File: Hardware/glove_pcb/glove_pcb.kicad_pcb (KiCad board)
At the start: 2 copper layers, 150 x 150 mm, 106 parts, among them J1 Barrel_Jack_Switch, J10 ICSP, J11 IMU, J12 IMU, J13 Conn_01x01, J2 Conn_01x02, J3 Conn_01x02, J4 Conn_01x02, J5 Conn_01x02, J6 Conn_01x02, J7 Potentiometers, J8 Potentiometers, J9 Debug Serial, U1 AP63205WU, U10 MCP3008, U11 MCP3008, U12 BM70BLES1FC2-0B04AA, U13 74LVC1T45GW_125, U14 74LVC1T45GW_125, U2 TCR2EF33_LMCT, U3 DRV8876PWPR, U4 DRV8876PWPR, U5 DRV8876PWPR, U6 DRV8876PWPR, U7 DRV8876PWPR, U8 MCP3008, U9 ATmega328PB-A

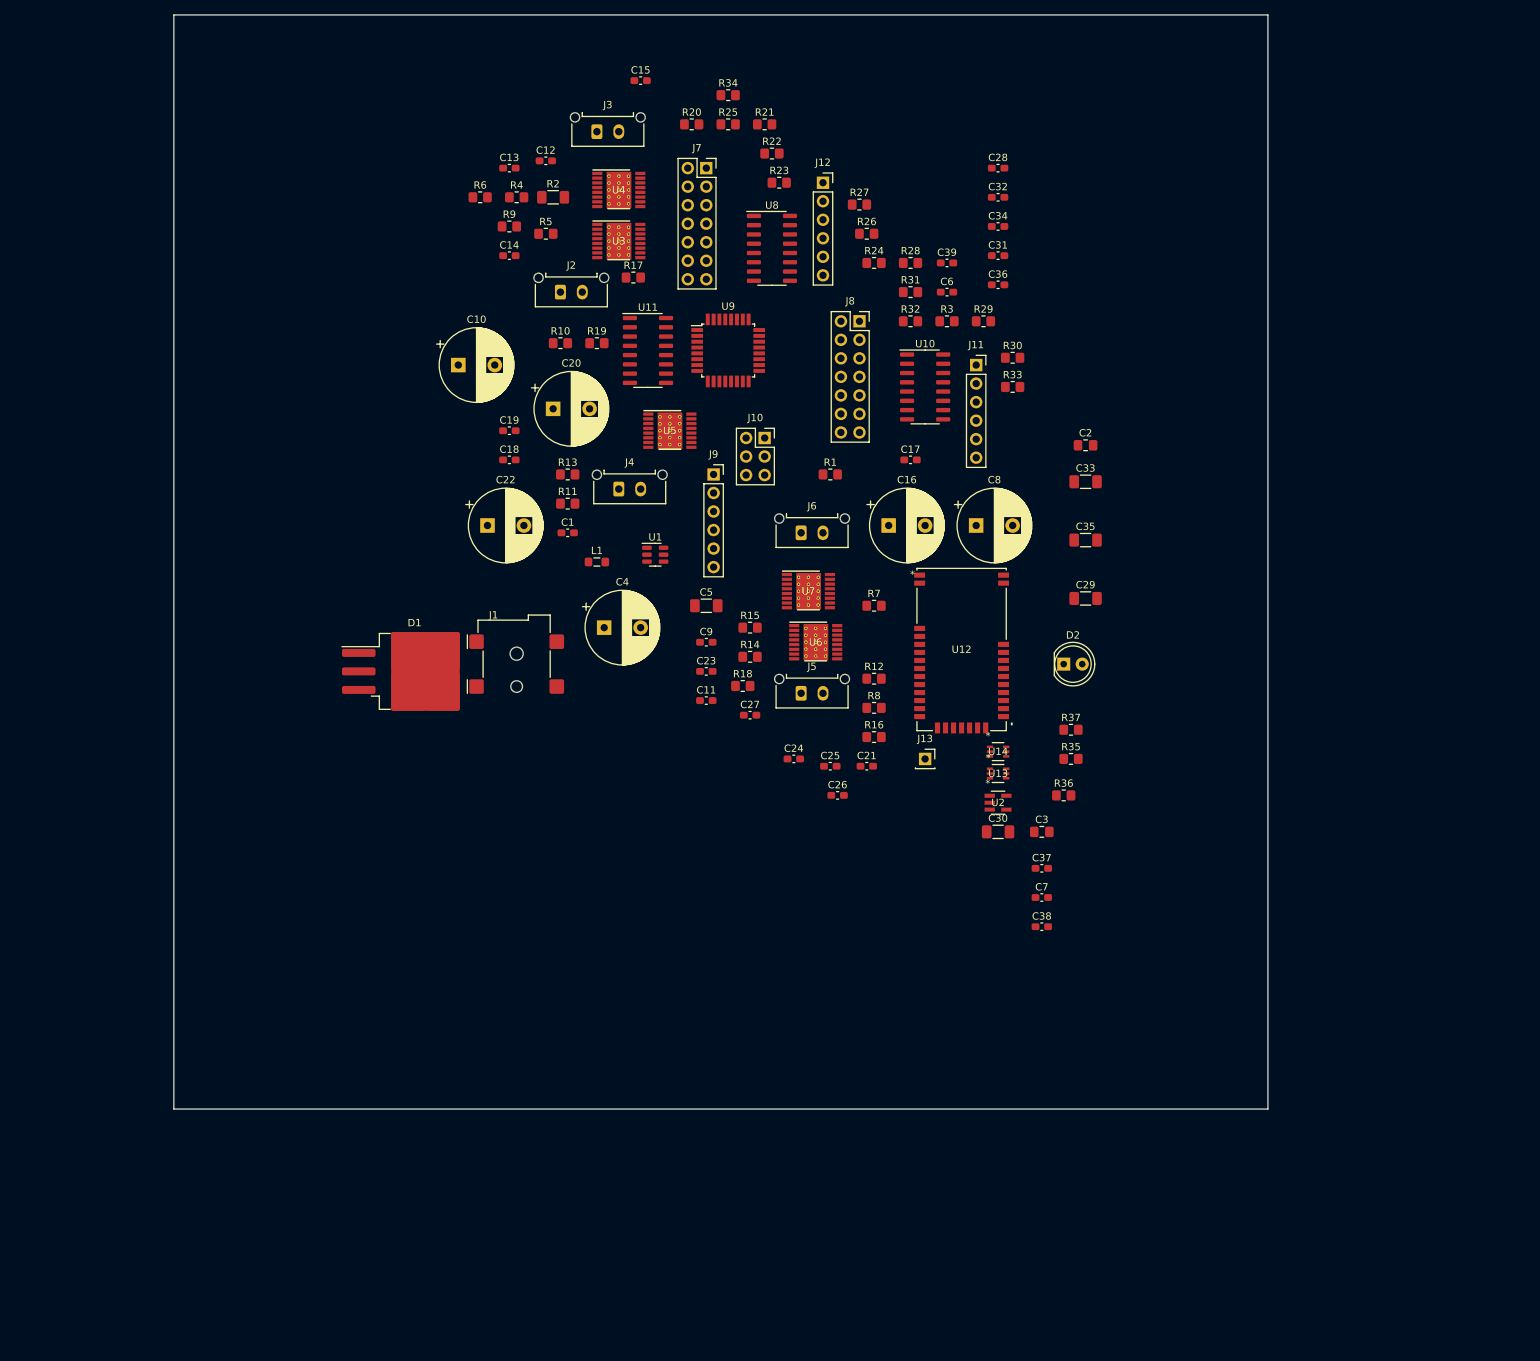
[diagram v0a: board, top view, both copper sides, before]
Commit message: Change barrel jack footprint and minor placing work
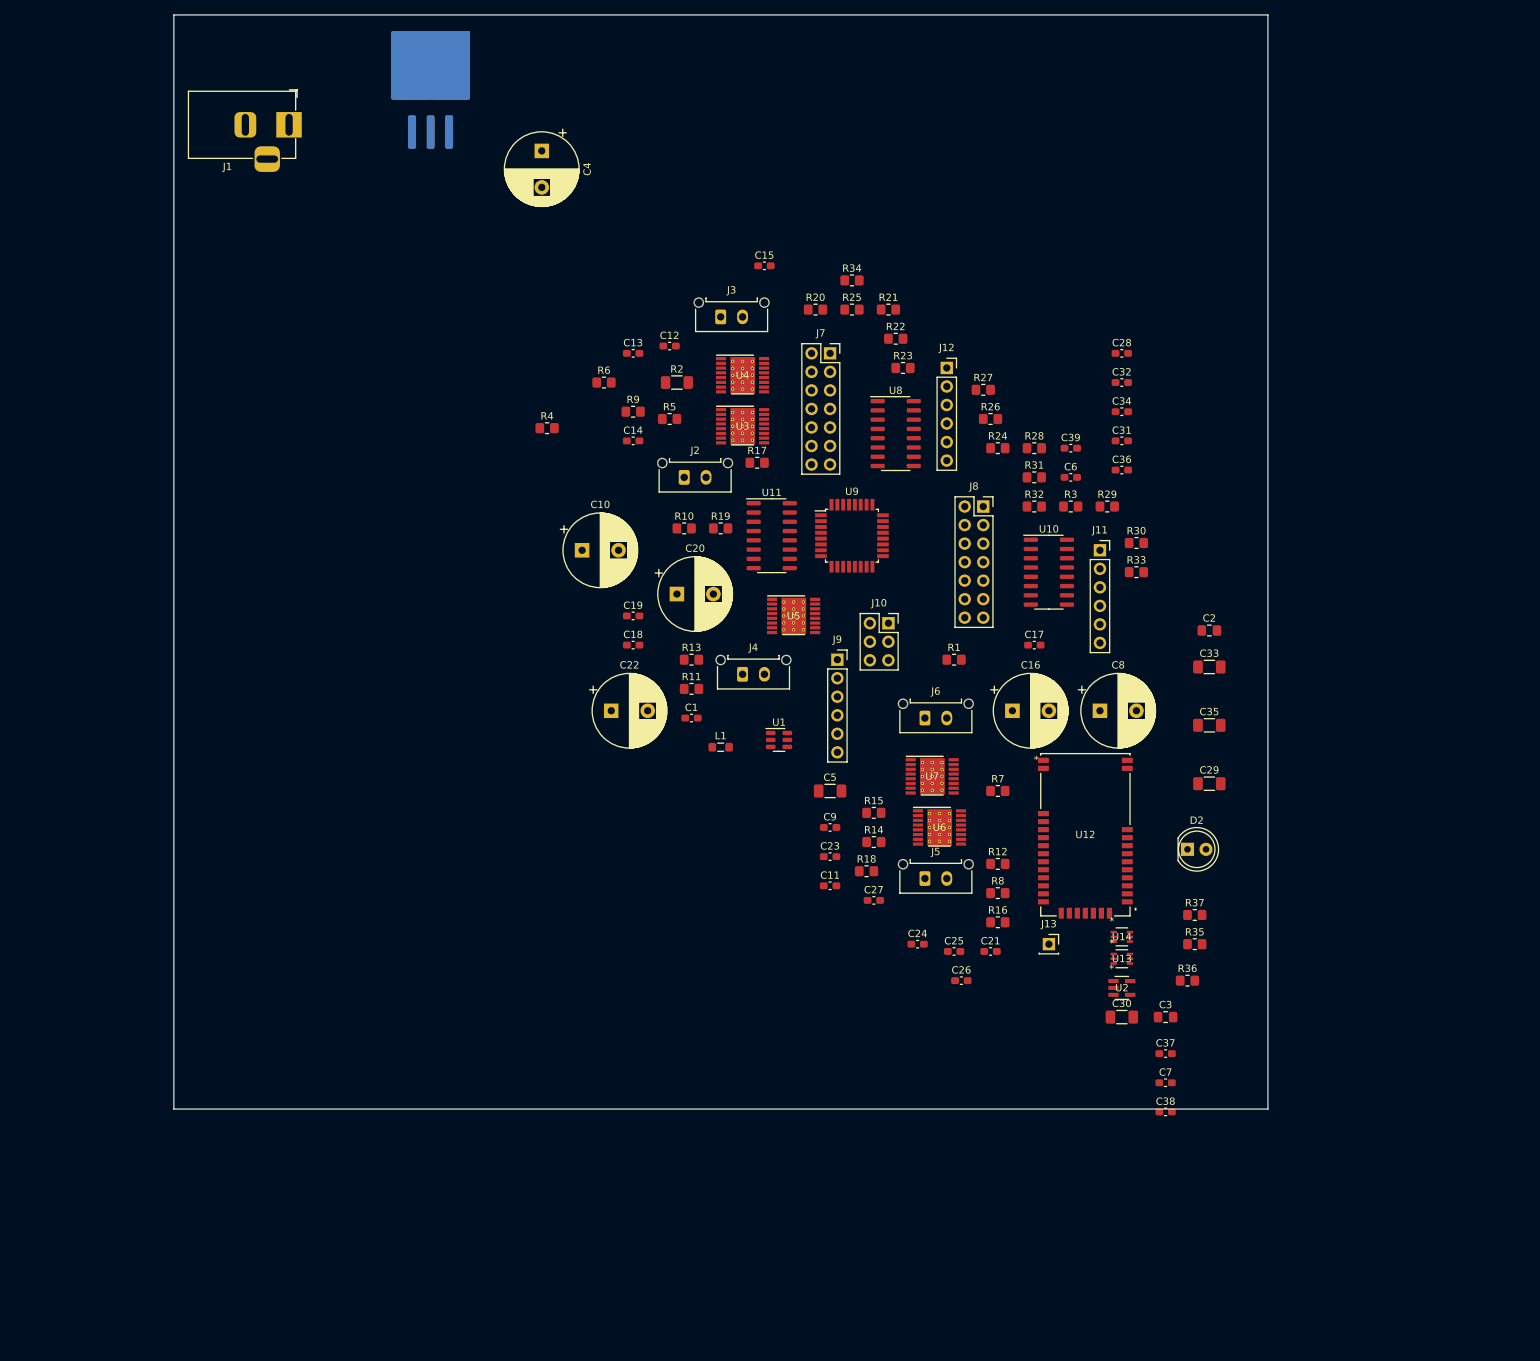
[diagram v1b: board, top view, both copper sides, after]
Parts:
- D1: moved to B.Cu
- J1: footprint Connector_BarrelJack:BarrelJack_Wuerth_694108106102_2.5x5.5mm -> Connector_BarrelJack:BarrelJack_Horizontal
- moved D1 81.6 mm to (76.2, 25.4), turned to 90 degrees
- moved J1 80.3 mm to (56.8, 32.1)
- moved C4 65.9 mm to (91.4, 35.6), turned to -90 degrees
- moved R4 31.9 mm to (92.2, 73.7)
- moved C11 30.5 mm to (131.0, 136.4)
- moved C21 30.5 mm to (153.0, 145.4)
- moved C23 30.5 mm to (131.0, 132.4)
- moved C24 30.5 mm to (143.0, 144.4)
- moved C25 30.5 mm to (148.0, 145.4)
- moved C26 30.5 mm to (149.0, 149.4)
- moved C27 30.5 mm to (137.0, 138.4)
- moved C3 30.5 mm to (177.0, 154.4)
- moved C30 30.5 mm to (171.0, 154.4)
- moved C37 30.5 mm to (177.0, 159.4)
- moved C38 30.5 mm to (177.0, 167.4)
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
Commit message: More partial placement of footprints
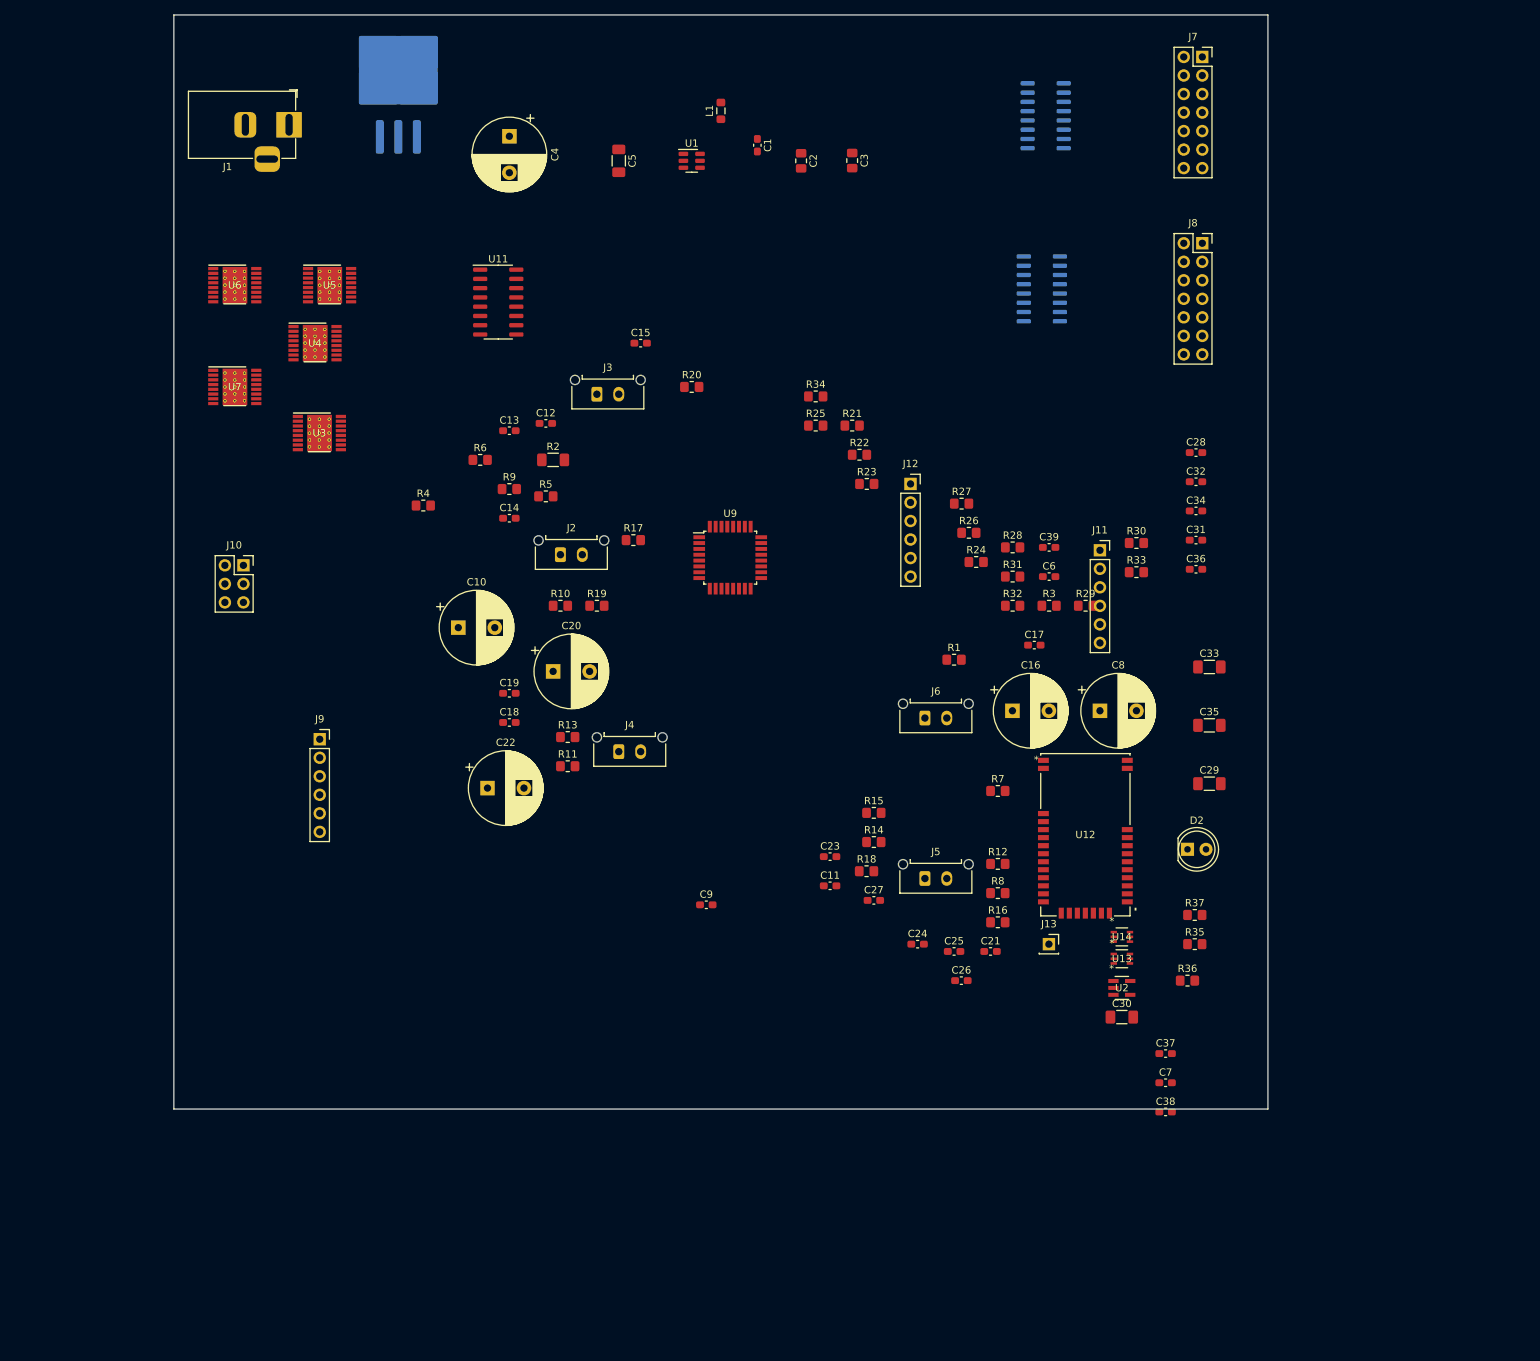
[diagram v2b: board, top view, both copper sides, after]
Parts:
- U10, U8: moved to B.Cu
- moved C3 125.0 mm to (134.0, 37.0), turned to -90 degrees
- moved U6 121.9 mm to (49.4, 54.0)
- moved U7 109.5 mm to (49.4, 68.0)
- moved C5 91.1 mm to (102.0, 37.0), turned to -90 degrees
- moved J10 88.8 mm to (50.5, 92.5)
- moved L1 87.2 mm to (116.0, 30.1), turned to 90 degrees
- moved C2 85.3 mm to (127.0, 37.0), turned to -90 degrees
- moved U1 80.3 mm to (112.0, 37.0)
- moved C1 79.0 mm to (121.0, 34.9), turned to -90 degrees
- moved U5 78.1 mm to (62.4, 54.0)
- moved J9 71.8 mm to (61.0, 116.3)
- moved J7 65.2 mm to (182.0, 22.8)
- moved U4 58.8 mm to (60.4, 62.0)
- moved U3 58.0 mm to (60.9, 74.3)
- moved U11 49.3 mm to (85.5, 56.4)
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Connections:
- D1 pad 1: MOTOR_VM -> (no net)
- D1 pad 2: Net-(D1-A) -> MOTOR_VM
- D1 pad 3: (no net) -> Net-(D1-A)

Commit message: Group up footprints with same location, not organized yet
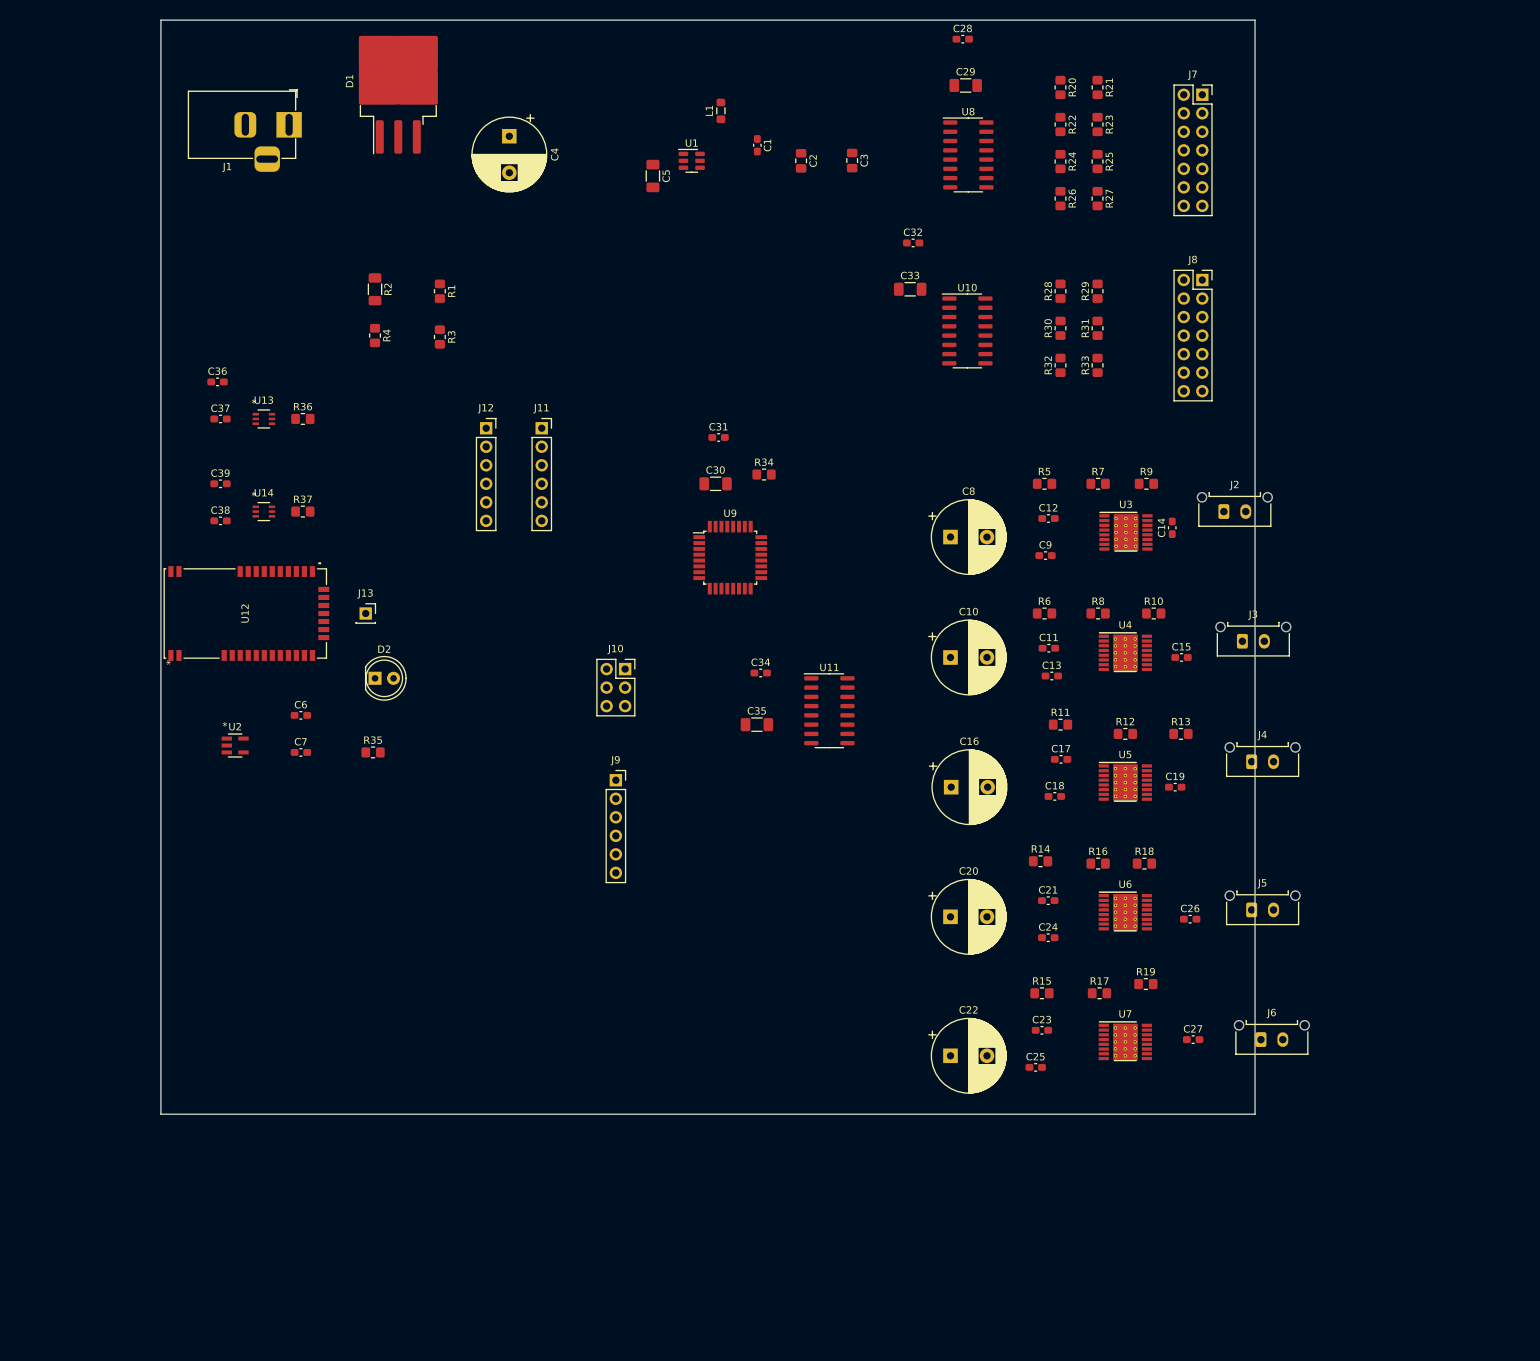
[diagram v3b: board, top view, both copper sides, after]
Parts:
- D1, U10, U8: moved to F.Cu
- moved C37 156.1 mm to (47.4, 72.4)
- moved C38 152.8 mm to (47.4, 86.4)
- moved U7 151.6 mm to (171.4, 157.8)
- moved U6 149.3 mm to (171.4, 140.0)
- moved R36 143.7 mm to (58.7, 72.4)
- moved U13 139.0 mm to (53.3, 72.4)
- moved C36 136.6 mm to (47.0, 67.3)
- moved R37 134.2 mm to (58.7, 85.1)
- moved U14 131.3 mm to (53.3, 85.1)
- moved U5 128.7 mm to (171.4, 122.2)
- moved C7 126.9 mm to (58.4, 118.1)
- moved U2 126.0 mm to (49.4, 117.2)
- moved U12 119.1 mm to (50.8, 99.1), turned to 90 degrees
- moved U4 118.9 mm to (171.4, 104.5)
- moved R35 115.7 mm to (68.3, 118.1)
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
